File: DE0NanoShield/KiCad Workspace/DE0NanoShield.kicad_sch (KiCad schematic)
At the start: 63 parts

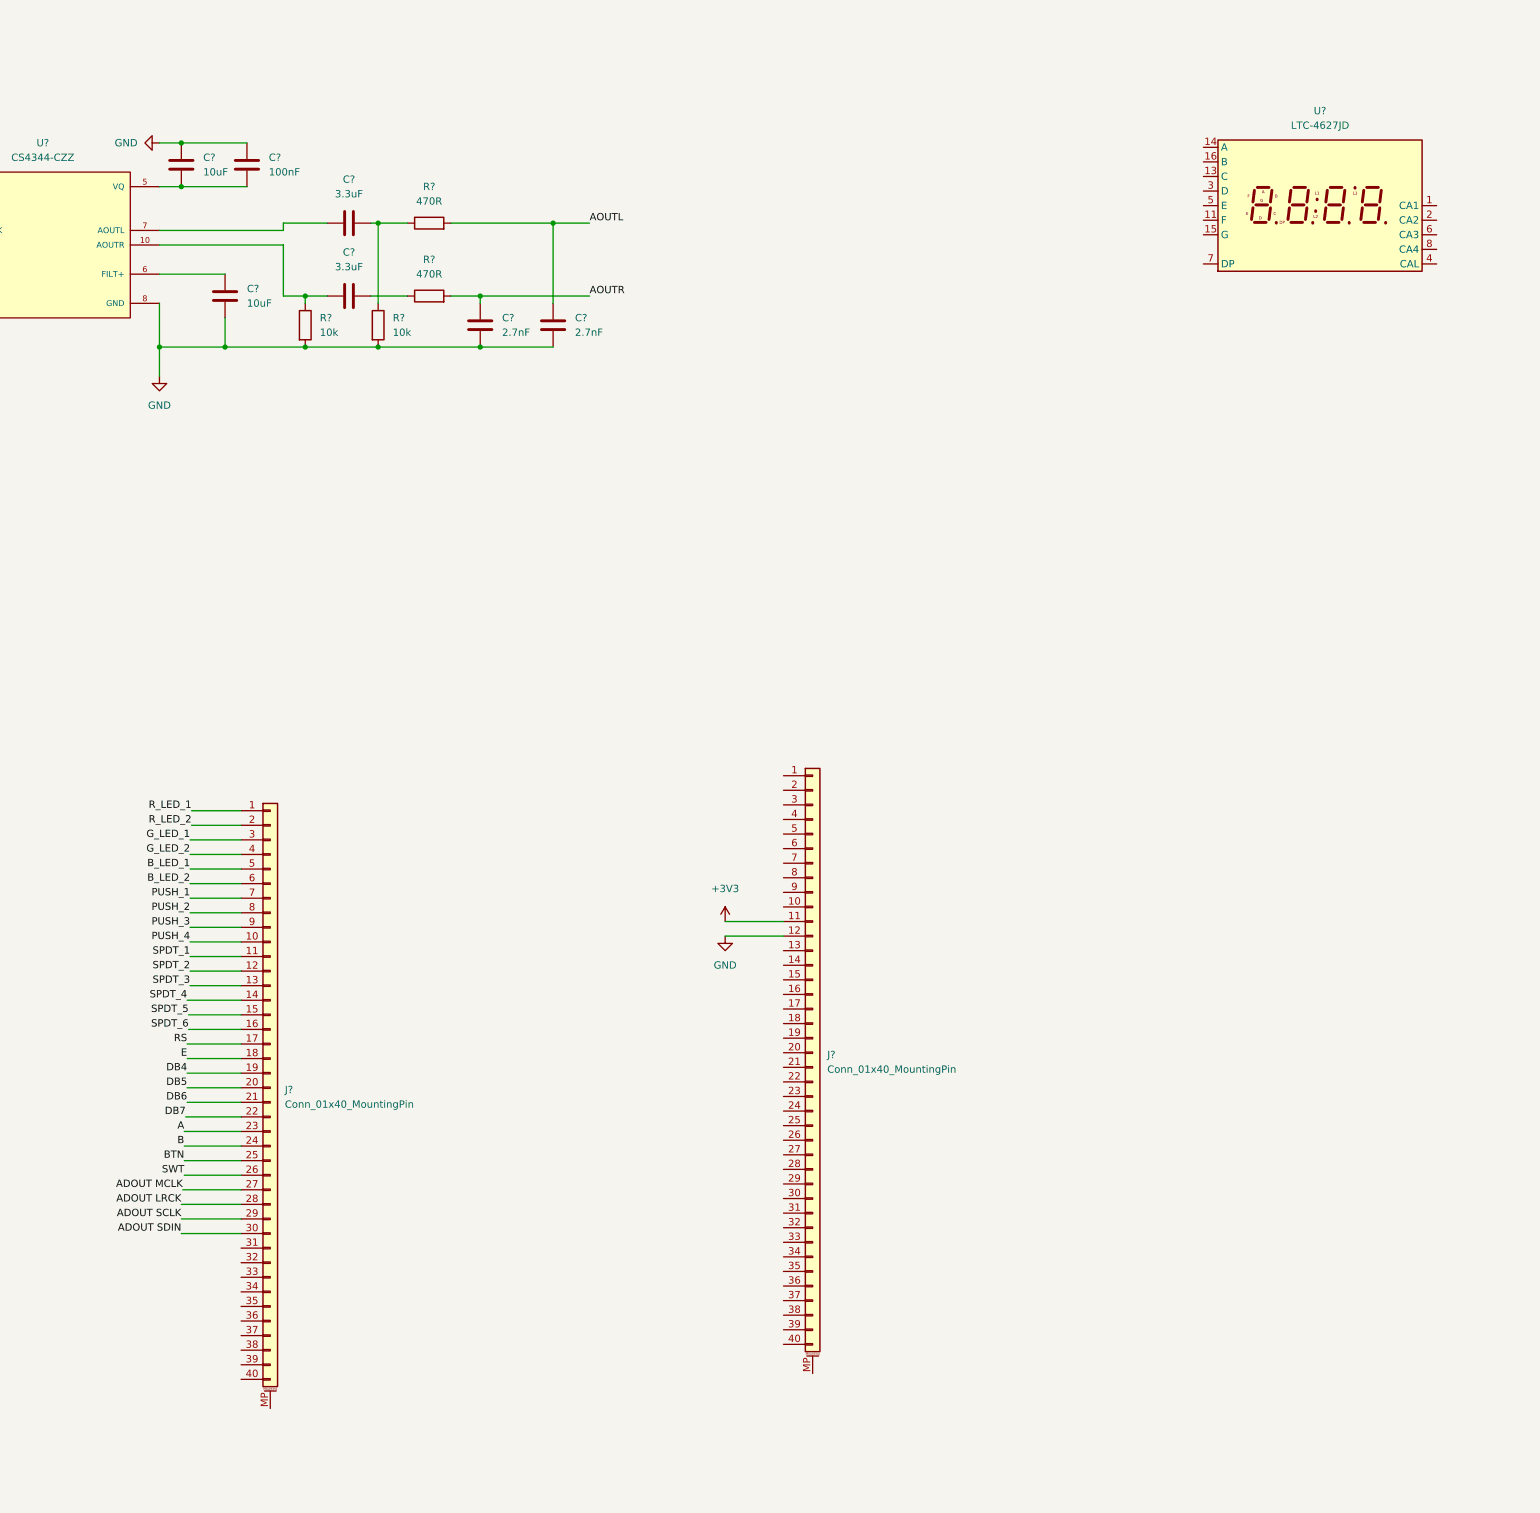
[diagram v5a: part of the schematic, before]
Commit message: Added hex display circuit
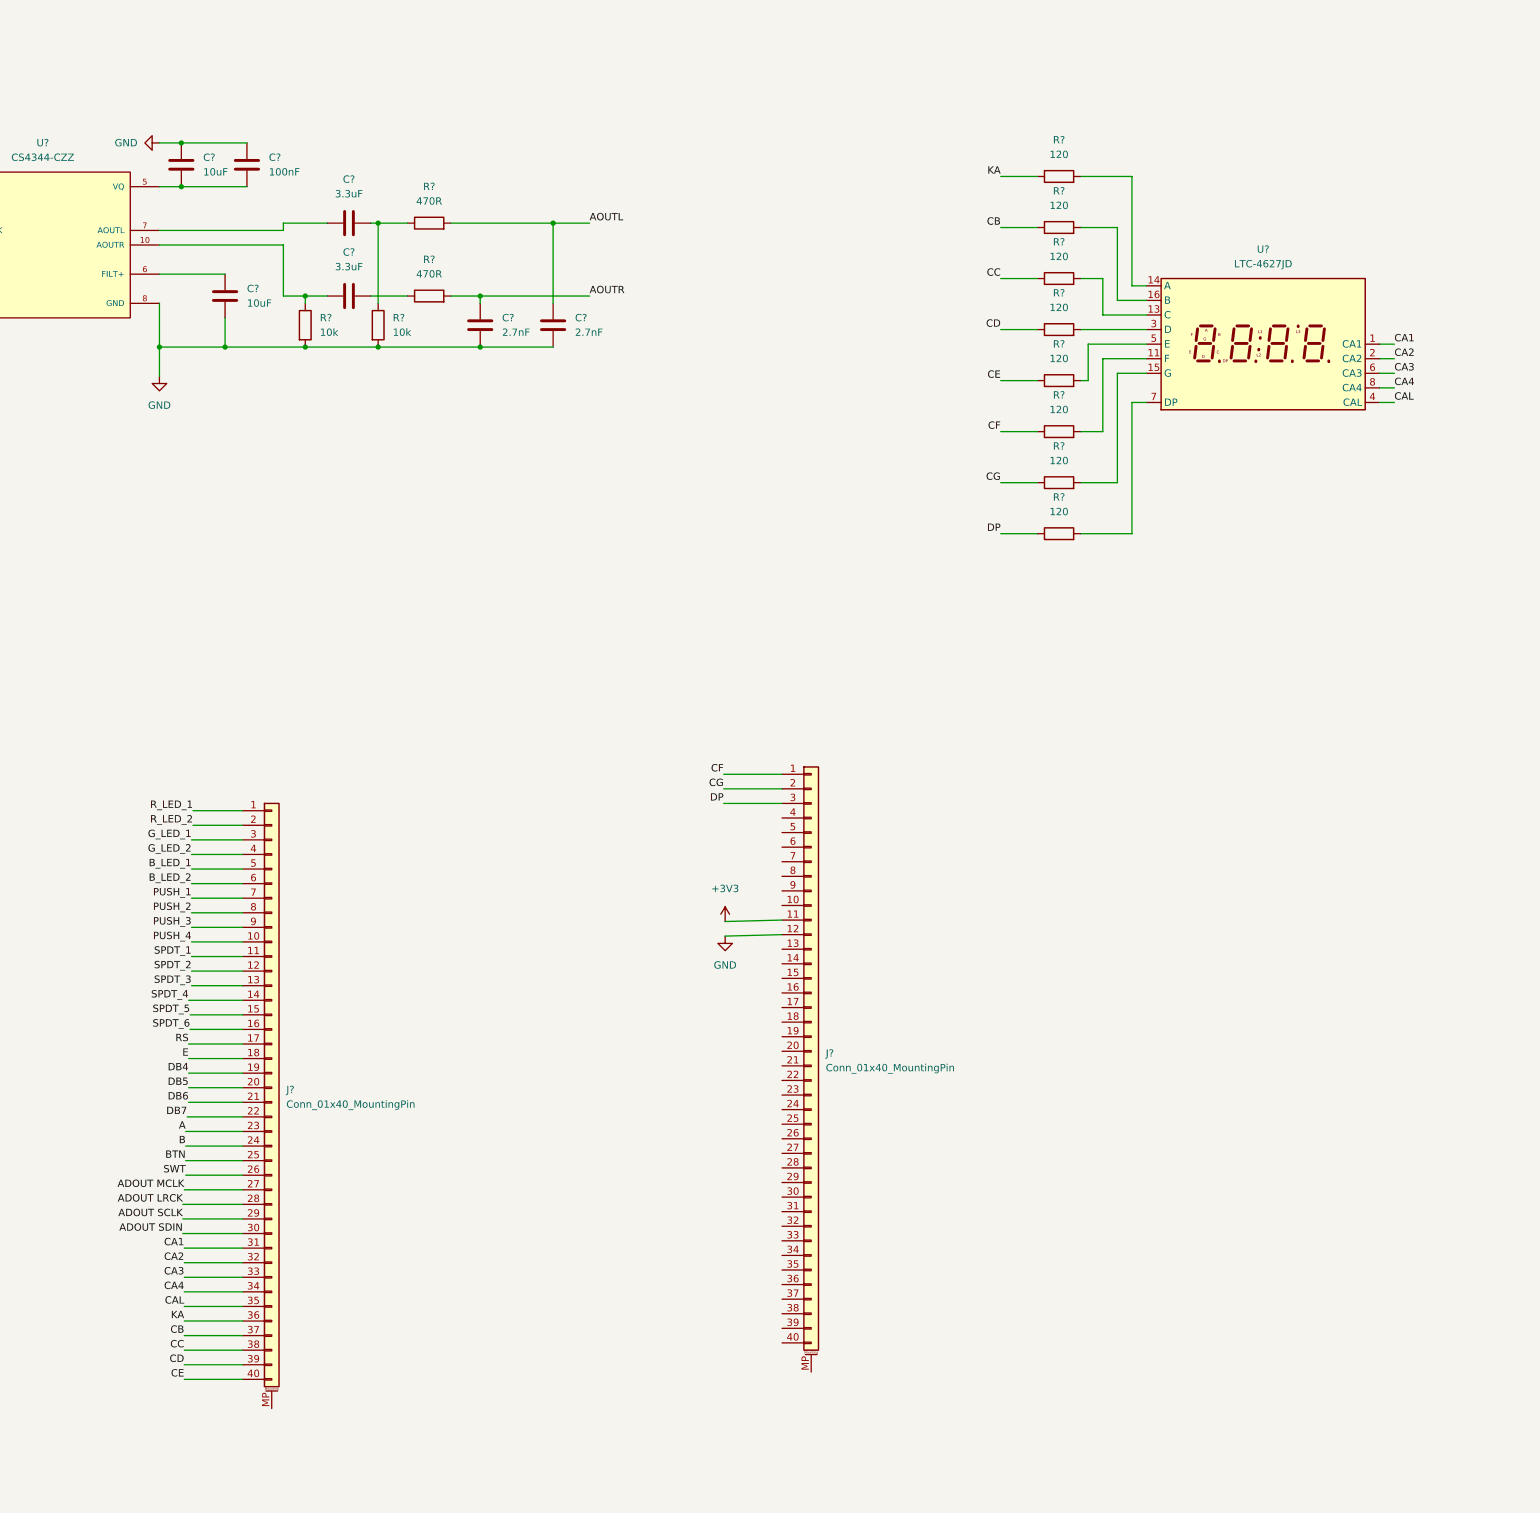
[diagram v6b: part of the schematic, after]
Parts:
- added R? (x8): 120, symbol Device:R
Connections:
- net CF: now reaches J?.1 (Pin_1)
- net CF: now also R?.1
- net CG: now reaches J?.2 (Pin_2)
- net CG: now also R?.1
- net DP: now reaches J?.3 (Pin_3)
- net DP: now also R?.1
- net CA1: now reaches J?.31 (Pin_31)
- net CA1: now also U?.1 (CA1)
- net CA2: now reaches J?.32 (Pin_32)
- net CA2: now also U?.2 (CA2)
- net CA3: now reaches J?.33 (Pin_33)
- net CA3: now also U?.6 (CA3)
- net CA4: now reaches J?.34 (Pin_34)
- net CA4: now also U?.8 (CA4)
- net CAL: now reaches J?.35 (Pin_35)
- net CAL: now also U?.4 (CAL)
- net KA: now reaches J?.36 (Pin_36)
- net KA: now also R?.1
- net CB: now reaches J?.37 (Pin_37)
- net CB: now also R?.1
- net CC: now reaches J?.38 (Pin_38)
- net CC: now also R?.1
- net CD: now reaches J?.39 (Pin_39)
- net CD: now also R?.1
- net CE: now reaches J?.40 (Pin_40)
- net CE: now also R?.1
- net at U?.11 (F): now also R?.2
- net at U?.13 (C): now also R?.2
- net at U?.14 (A): now also R?.2
- net at U?.15 (G): now also R?.2
- net at U?.16 (B): now also R?.2
- net at U?.3 (D): now also R?.2
- net at U?.5 (E): now also R?.2
- net at U?.7 (DP): now also R?.2
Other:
- moved on the sheet: U?

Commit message: added pmod connections
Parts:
- added J? (x3): Conn_01x06_MountingPin, symbol Connector_Generic_MountingPin:Conn_01x06_MountingPin
- added J?: Conn_01x12_MountingPin, symbol Connector_Generic_MountingPin:Conn_01x12_MountingPin
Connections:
- net +3V3: now also J?.12 (Pin_12), J?.6 (Pin_6), J?.6 (Pin_6), J?.6 (Pin_6), J?.6 (Pin_6)
- net CD: now also J?.30 (Pin_30), J?.9 (Pin_9)
- net GND: now also J?.11 (Pin_11), J?.5 (Pin_5), J?.5 (Pin_5), J?.5 (Pin_5), J?.5 (Pin_5)
- net DAT1: now reaches J?.28 (Pin_28)
- net DAT1: now also J?.7 (Pin_7)
- net DAT2: now reaches J?.29 (Pin_29)
- net DAT2: now also J?.8 (Pin_8)
- net SCK: now reaches J?.31 (Pin_31)
- net SCK: now also J?.4 (Pin_4)
- net CS3: now reaches J?.32 (Pin_32)
- net CS3: now also J?.1 (Pin_1)
- net CS2: now reaches J?.33 (Pin_33)
- net CS2: now also J?.1 (Pin_1)
- net MOSI: now reaches J?.34 (Pin_34)
- net MOSI: now also J?.38 (Pin_38), J?.2 (Pin_2), J?.2 (Pin_2), J?.2 (Pin_2)
- net MISO: now reaches J?.35 (Pin_35)
- net MISO: now also J?.3 (Pin_3), J?.3 (Pin_3)
- net SCLK: now reaches J?.36 (Pin_36)
- net SCLK: now also J?.39 (Pin_39), J?.4 (Pin_4), J?.4 (Pin_4)
- net CS1: now reaches J?.37 (Pin_37)
- net CS1: now also J?.1 (Pin_1)
- net RTS: now reaches J?.4 (Pin_4)
- net RTS: now also J?.1 (Pin_1)
- net RXD: now reaches J?.5 (Pin_5)
- net RXD: now also J?.2 (Pin_2)
- net TXD: now reaches J?.6 (Pin_6)
- net TXD: now also J?.3 (Pin_3)
- net CTS: now reaches J?.7 (Pin_7)
- net CTS: now also J?.4 (Pin_4)
- no-connect marks 4 -> 6
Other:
- moved on the sheet: 10k, C?, D?, FL?, J?, R?, RV?, SW?, U?

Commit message: annotated schematic and added footprints
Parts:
- added J8: Conn_01x08_Female, Connector_JST:JST_EH_B8B-EH-A_1x08_P2.50mm_Vertical, symbol Connector:Conn_01x08_Female
- C1, C3, C4, C5, C6: renamed from C?; footprint (none) -> Capacitor_SMD:C_0603_1608Metric
- C10, C2, C7, C8, C9: renamed from C?; footprint (none) -> Capacitor_SMD:C_0402_1005Metric
- D1, D2, D3, D4, D5, D6: renamed from D?; footprint (none) -> LED_SMD:LED_0603_1608Metric
- J1, J2: renamed from J?; footprint (none) -> Connector_FFC-FPC:Hirose_FH12-40S-0.5SH_1x40-1MP_P0.50mm_Horizontal
- J3: renamed from J?; footprint (none) -> Connector_JST:JST_PH_B16B-PH-K_1x16_P2.00mm_Vertical
- J4, J5, J6: renamed from J?; footprint (none) -> Connector_JST:JST_GH_SM06B-GHS-TB_1x06-1MP_P1.25mm_Horizontal
- J7: renamed from J?; footprint (none) -> Connector_JST:JST_GH_SM12B-GHS-TB_1x12-1MP_P1.25mm_Horizontal
- R1, R2, R3, R4: renamed from 10k; value R -> 10k; footprint (none) -> Resistor_SMD:R_0603_1608Metric
- R10, R5, R6, R7, R8, R9: renamed from R?; value R -> 10k; footprint (none) -> Resistor_SMD:R_0603_1608Metric
- R11, R12, R13, R14, R15, R16, R17, R18, R19, R20, R21, R22, R23, R24, R30: renamed from R?; footprint (none) -> Resistor_SMD:R_0402_1005Metric
- R25, R26, R27, R28, R29, R31, R32, R36: renamed from R?; footprint (none) -> Resistor_SMD:R_0603_1608Metric
- R33, R34: renamed from R?; footprint (none) -> Resistor_SMD:R_0612_1632Metric
- R35: renamed from R?; value 1 -> 10k; footprint (none) -> Resistor_SMD:R_0603_1608Metric
- RV1: renamed from RV?; footprint (none) -> Potentiometer_SMD:Potentiometer_Bourns_3224W_Vertical
- SW1, SW10, SW12, SW3, SW4, SW8, SW9: renamed from SW?; footprint (none) -> Button_Switch_SMD:SW_SPDT_PCM12
- SW2, SW5, SW6, SW7: renamed from SW?; footprint (none) -> Button_Switch_SMD:SW_Push_SPST_NO_Alps_SKRK
- gave numbers to parts that had none: 4
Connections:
- net +5V is gone; now on net +3V3: J3.15 (Pin_15), J3.2 (Pin_2), RV1.3
- net Y4: now reaches J2.16 (Pin_16)
- net Y4: now also J8.1 (Pin_1)
- net Y3: now reaches J2.17 (Pin_17)
- net Y3: now also J8.2 (Pin_2)
- net Y2: now reaches J2.18 (Pin_18)
- net Y2: now also J8.3 (Pin_3)
- net Y1: now reaches J2.19 (Pin_19)
- net Y1: now also J8.4 (Pin_4)
- net X4: now reaches J2.20 (Pin_20)
- net X4: now also J8.5 (Pin_5)
- net X3: now reaches J2.21 (Pin_21)
- net X3: now also J8.6 (Pin_6)
- net X2: now reaches J2.22 (Pin_22)
- net X2: now also J8.7 (Pin_7)
- net X1: now reaches J2.23 (Pin_23)
- net X1: now also J8.8 (Pin_8)
- no-connect marks 6 -> 23
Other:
- note added: "40 pin breakout - 1st"
- note added: "40 pin breakout - 2nd"
- note added: "4X4 KeyPad"
- note added: "4x4 Matrix Keypad"
- note added: "AD5"
- note added: "Additional Peripherials"
- note added: "Audio Output"
- note added: "DA4"
- note added: "DEO-nano Breakout"
- note added: "HEX Display"
- note added: "LCD"
- note added: "LEDs"
- note added: "Pmod Connectors"
- note added: "Push Buttons"
- note added: "Rotary Encoder"
- note added: "SD Card"
- note added: "SPDT Buttons"
- note added: "Trimmer for tuning LCD Brightness"
- note added: "USB"
- title: (none) -> DE0-Nano Shield
- moved on the sheet: C1, C10, C2, C3, C4, C5, C6, C7, C8, C9, D1, D2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
